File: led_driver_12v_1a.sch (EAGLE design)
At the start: 35 parts, among them Q1 BSZ0902NSI, Q2 BSZ0902NSI, Q3 BSZ0902NSI, Q4 BSZ0902NSI, Q5 BSZ0902NSI

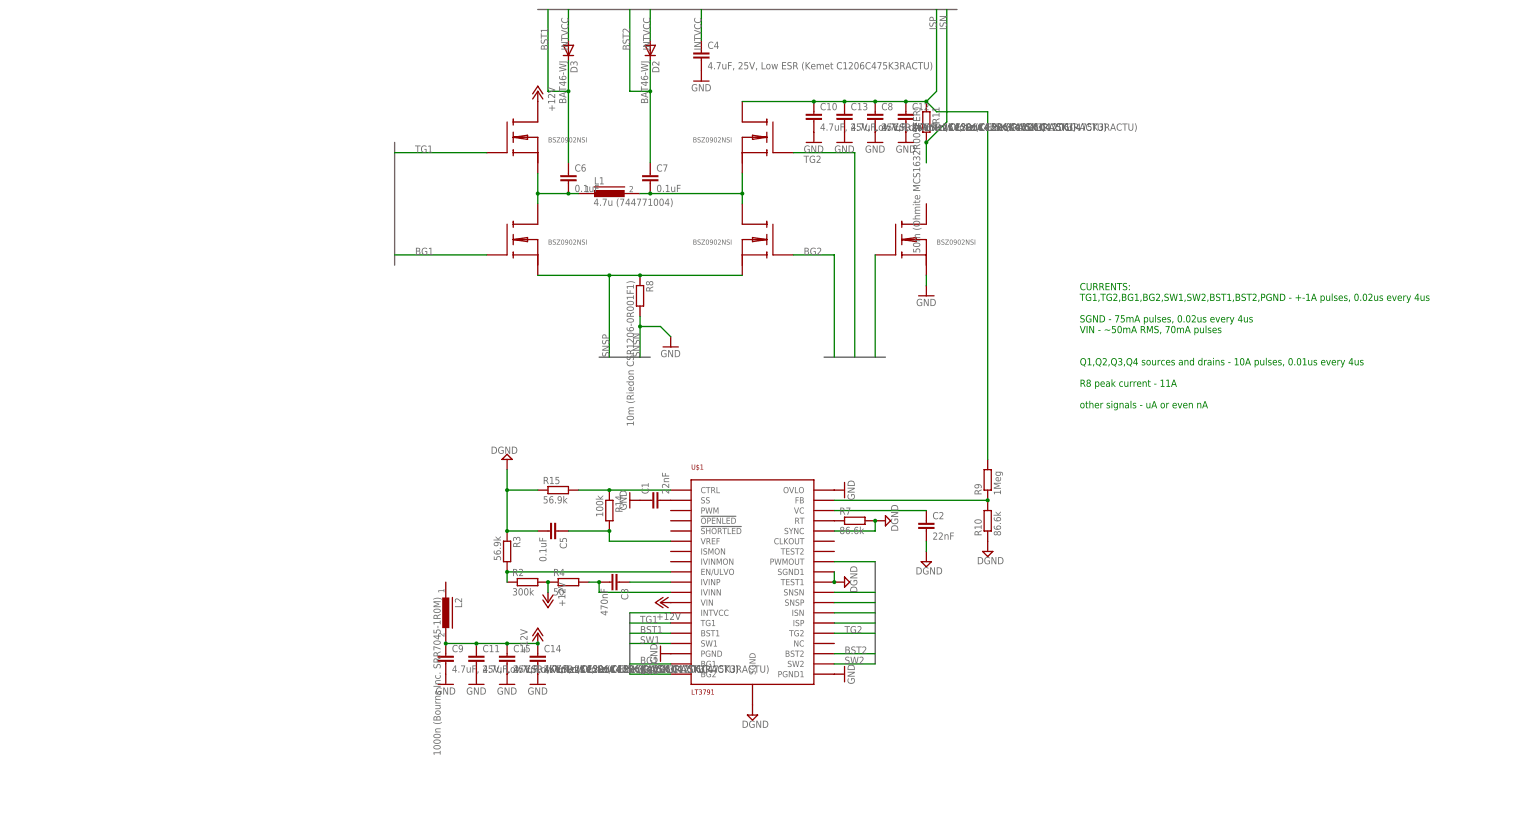
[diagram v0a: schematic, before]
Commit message: schematics roughly finished, components are roughly in place. Need accurate routing and fine component adjustments
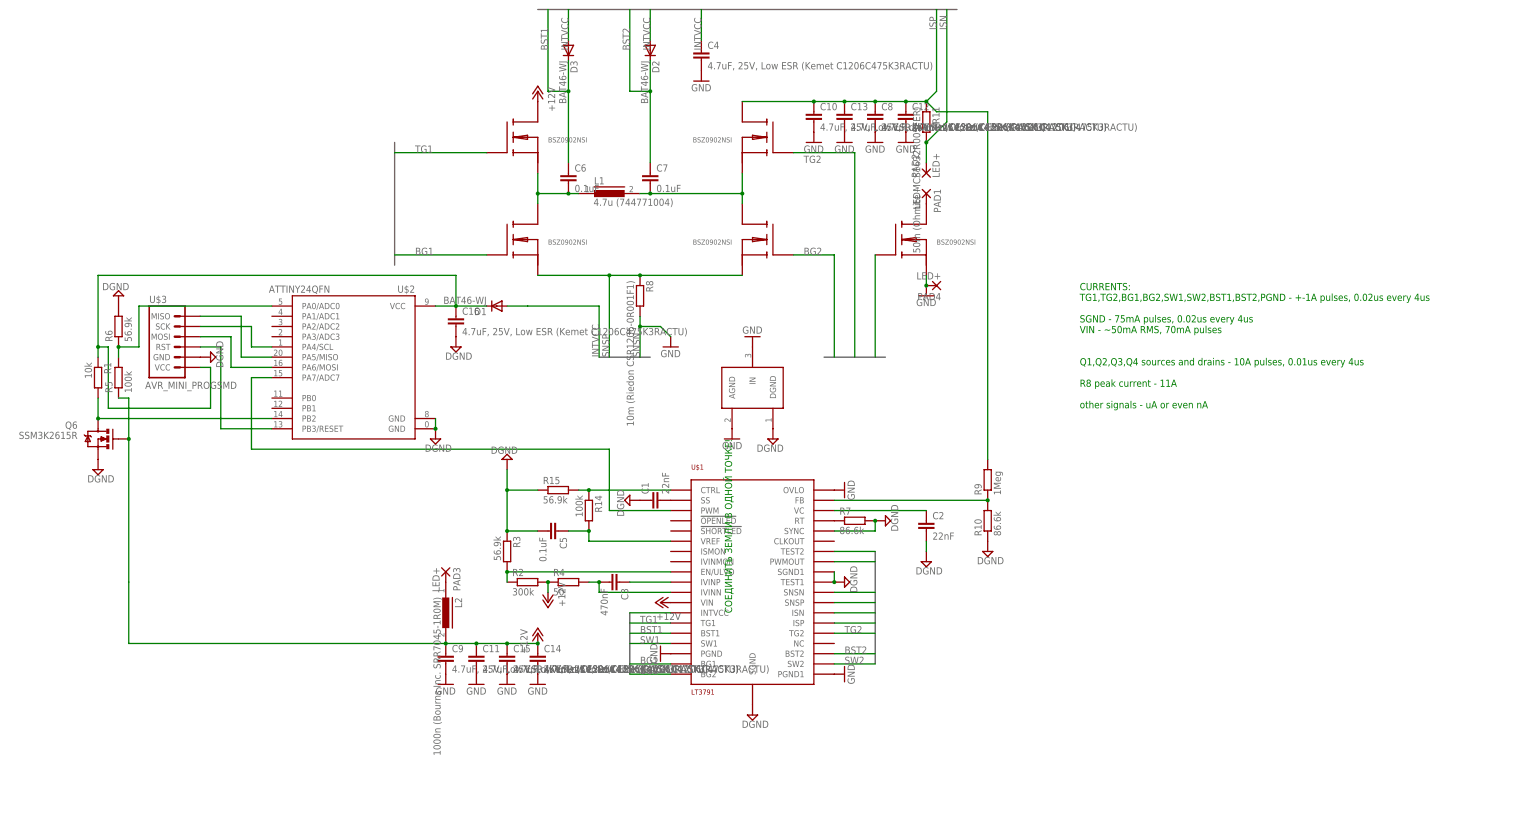
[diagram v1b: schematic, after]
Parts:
- added C16: 4.7uF, 25V, Low ESR (Kemet C1206C475K3RACTU), rcl:C-EUC1206
- added D1: BAT46-WJ, diode:DIODE-SOD323-W
- added PAD1: LED-, wirepad:WIREPADSMD5-2,5
- added PAD2, PAD3, PAD4: LED+, wirepad:WIREPADSMD5-2,5
- added Q6: SSM3K2615R, SparkFun-DiscreteSemi:MOSFET-NCHANNELBSS123LT1G
- added R1: 10k, resistor:R-EU_R0402
- added R5: 100k, resistor:R-EU_R0402
- added R6: 56.9k, resistor:R-EU_R0402
- added U$2: ATTINY24QFN, SparkFun-DigitalIC:ATTINY24QFN
- added U$3: AVR_MINI_PROGSMD, SparkFun-Connectors:AVR_MINI_PROGSMD
- added U$4: GND_CONNECT, SparkFun-Passives:GND_CONNECT
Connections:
- new net N$12: C16.1, D1.C, R1.1, U$2.VCC, U$3.VCC
- new net N$13: Q6.D, R1.2, U$2.PB2
- new net N$14: U$1.PWM, U$2.PA7/ADC7
- new net N$15: R5.2, R6.1, U$2.PA0/ADC0
- new net N$16: U$2.PA5/MISO, U$3.MISO
- new net N$17: U$2.PA6/MOSI, U$3.MOSI
- new net N$18: U$2.PB3/RESET, U$3.RST
- new net N$19: PAD1.P, Q5.D
- new net N$20: U$2.PA4/SCL, U$3.SCK
- new net N$21: L2.1, PAD3.P
- net +12V: now also Q6.G, R5.1
- net DGND: now also C1.1, C16.2, Q6.S, R6.2, U$2.GND, U$2.GND@0, U$3.GND, U$4.DGND
- net GND: now also PAD4.P, U$4.AGND, U$4.IN; no longer C1.1
- net INTVCC: now also D1.A, U$1.TEST2
- net ISN: now also PAD2.P
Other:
- note added: "СОЕДИНИТЬ ЗЕМЛИ В ОДНОЙ ТОЧКЕ!"
- moved on the sheet: R14

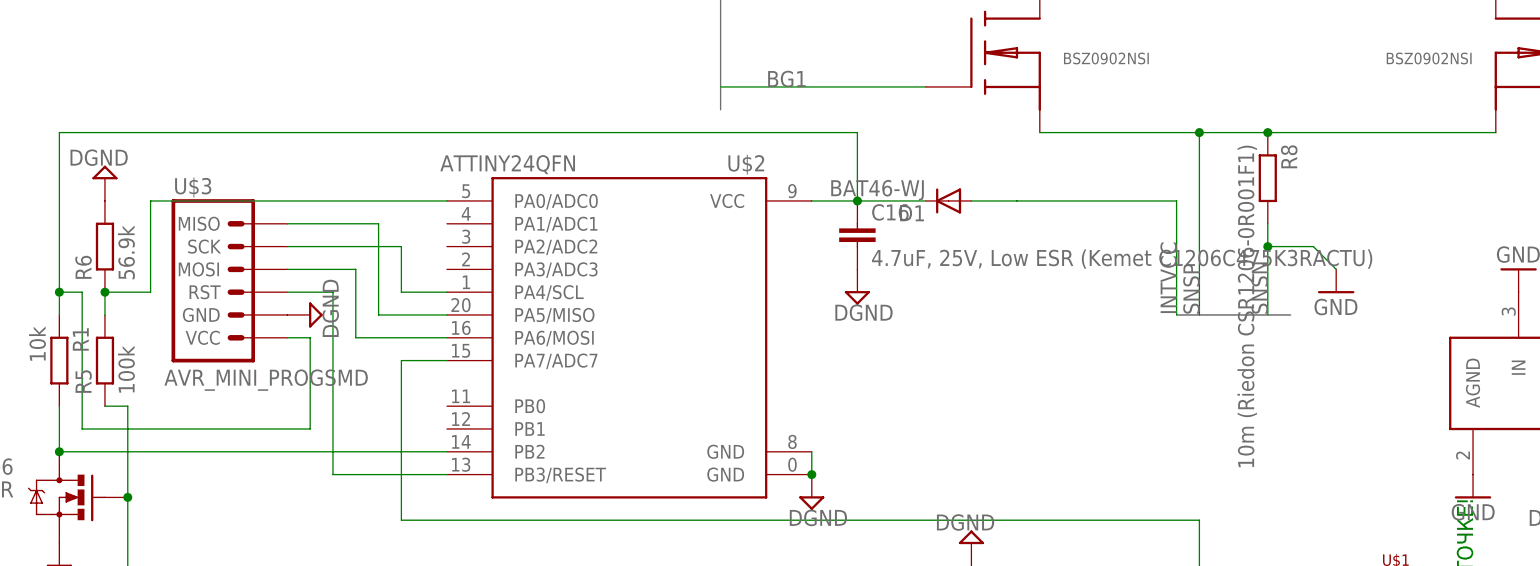
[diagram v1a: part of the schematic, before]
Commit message: second iteration of component placement. already have routing improvements, but still plenty of work to do
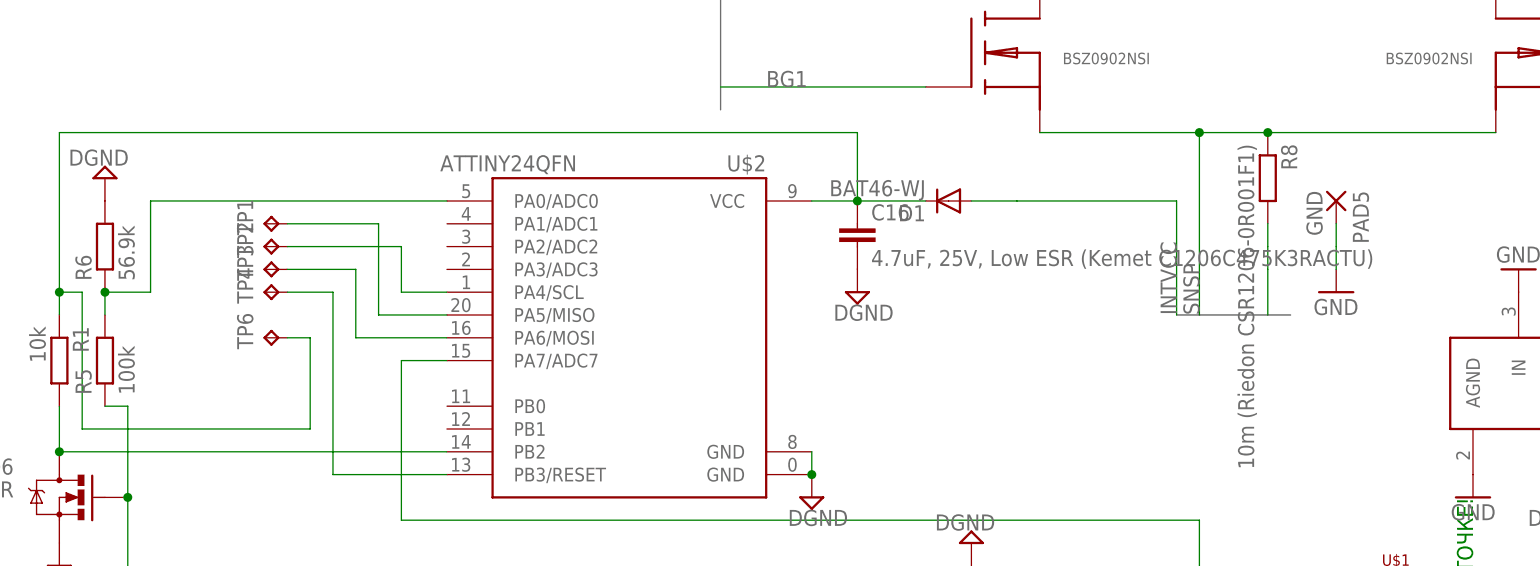
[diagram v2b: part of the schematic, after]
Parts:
- removed U$3: AVR_MINI_PROGSMD, SparkFun-Connectors:AVR_MINI_PROGSMD
- added PAD5: GND, wirepad:WIREPADSMD1,27-254
- added TP1, TP2, TP3, TP4, TP6: TPTP11R, testpad:TPTP11R
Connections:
- net DGND: no longer U$3.GND
- net GND: now also PAD5.P
- net N$12: now also TP6.TP; no longer U$3.VCC
- net N$16: now also TP1.TP; no longer U$3.MISO
- net N$17: now also TP3.TP; no longer U$3.MOSI
- net N$18: now also TP4.TP; no longer U$3.RST
- net N$20: now also TP2.TP; no longer U$3.SCK

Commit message: routing complete. main tasks to do: add polys, optimize routes width, add some extra vias, make gerbers
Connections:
- removed net N$10: C7.2, L1.2, Q3.D, Q4.S
- removed net N$8: C6.2, L1.1, Q1.S, Q2.D
- net SNSN: now also R8.1; no longer R8.2
- net SNSP: now also R8.2; no longer R8.1
- net SW1: now also C6.2, L1.1, Q1.S, Q2.D
- net SW2: now also C7.2, L1.2, Q3.D, Q4.S
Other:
- moved on the sheet: R8
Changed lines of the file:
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@@
 <clearance class="0" value="0.1524"/>
 </class>
-<class number="1" name="HI_PWR" width="0.3" drill="0.5">
+<class number="1" name="HI_PWR" width="0.3" drill="0.4">
 <clearance class="1" value="0.15"/>
 </class>
@@
 <instance part="Q3" gate="G$1" x="5.08" y="50.8" rot="MR0"/>
 <instance part="Q5" gate="G$1" x="45.72" y="50.8"/>
-<instance part="R8" gate="G$1" x="-22.86" y="38.1" rot="R270"/>
+<instance part="R8" gate="G$1" x="-22.86" y="35.56" rot="R90"/>
 <instance part="R11" gate="G$1" x="48.26" y="81.28" rot="R270"/>
 <instance part="D2" gate="G$1" x="-20.32" y="99.06" rot="R270"/>
@@
 <wire x1="25.4" y1="48.26" x2="25.4" y2="22.86" width="0.1524" layer="91"/>
 <label x="17.78" y="48.26" size="1.778" layer="95"/>
+<label x="25.4" y="25.4" size="1.778" layer="95" rot="R90"/>
 </segment>
 </net>
@@
 </segment>
 </net>
-<net name="SW2" class="0">
+<net name="SW2" class="1">
 <segment>
 <pinref part="U$1" gate="G$1" pin="SW2"/>
@@
 <label x="27.94" y="-53.34" size="1.778" layer="95"/>
 </segment>
-</net>
-<net name="SW1" class="0">
+<segment>
+<pinref part="L1" gate="G$1" pin="2"/>
+<pinref part="C7" gate="G$1" pin="2"/>
+<wire x1="-22.86" y1="63.5" x2="-20.32" y2="63.5" width="0.1524" layer="91"/>
+<pinref part="Q4" gate="G$1" pin="S"/>
+<wire x1="-20.32" y1="63.5" x2="2.54" y2="63.5" width="0.1524" layer="91"/>
+<wire x1="2.54" y1="63.5" x2="2.54" y2="68.58" width="0.1524" layer="91"/>
+<junction x="-20.32" y="63.5"/>
+<pinref part="Q3" gate="G$1" pin="D"/>
+<wire x1="2.54" y1="63.5" x2="2.54" y2="60.96" width="0.1524" layer="91"/>
+<junction x="2.54" y="63.5"/>
+<wire x1="27.94" y1="22.86" x2="27.94" y2="63.5" width="0.1524" layer="91"/>
+<wire x1="27.94" y1="63.5" x2="2.54" y2="63.5" width="0.1524" layer="91"/>
+<label x="27.94" y="25.4" size="1.778" layer="95" rot="R90"/>
+</segment>
+</net>
+<net name="SW1" class="1">
 <segment>
 <pinref part="U$1" gate="G$1" pin="SW1"/>
 <wire x1="-15.24" y1="-48.26" x2="-25.4" y2="-48.26" width="0.1524" layer="91"/>
 <label x="-22.86" y="-48.26" size="1.778" layer="95"/>
+</segment>
+<segment>
+<pinref part="Q1" gate="G$1" pin="S"/>
+<pinref part="Q2" gate="G$1" pin="D"/>
+<wire x1="-48.26" y1="68.58" x2="-48.26" y2="63.5" width="0.1524" layer="91"/>
+<pinref part="L1" gate="G$1" pin="1"/>
+<wire x1="-48.26" y1="63.5" x2="-48.26" y2="60.96" width="0.1524" layer="91"/>
+<wire x1="-38.1" y1="63.5" x2="-40.64" y2="63.5" width="0.1524" layer="91"/>
+<junction x="-48.26" y="63.5"/>
+<pinref part="C6" gate="G$1" pin="2"/>
+<wire x1="-40.64" y1="63.5" x2="-48.26" y2="63.5" width="0.1524" layer="91"/>
+<junction x="-40.64" y="63.5"/>
+<wire x1="-83.82" y1="63.5" x2="-48.26" y2="63.5" width="0.1524" layer="91"/>
+<label x="-78.74" y="63.5" size="1.778" layer="95"/>
 </segment>
 </net>
@@
 <wire x1="30.48" y1="73.66" x2="30.48" y2="22.86" width="0.1524" layer="91"/>
 <label x="17.78" y="71.12" size="1.778" layer="95"/>
+<label x="30.48" y="25.4" size="1.778" layer="95" rot="R90"/>
 </segment>
 </net>
@@
 </segment>
 </net>
-<net name="N$8" class="1">
-<segment>
-<pinref part="Q1" gate="G$1" pin="S"/>
-<pinref part="Q2" gate="G$1" pin="D"/>
-<wire x1="-48.26" y1="68.58" x2="-48.26" y2="63.5" width="0.1524" layer="91"/>
-<pinref part="L1" gate="G$1" pin="1"/>
-<wire x1="-48.26" y1="63.5" x2="-48.26" y2="60.96" width="0.1524" layer="91"/>
-<wire x1="-38.1" y1="63.5" x2="-40.64" y2="63.5" width="0.1524" layer="91"/>
-<junction x="-48.26" y="63.5"/>
-<pinref part="C6" gate="G$1" pin="2"/>
-<wire x1="-40.64" y1="63.5" x2="-48.26" y2="63.5" width="0.1524" layer="91"/>
-<junction x="-40.64" y="63.5"/>
-</segment>
-</net>
-<net name="N$10" class="1">
-<segment>
-<pinref part="L1" gate="G$1" pin="2"/>
-<pinref part="C7" gate="G$1" pin="2"/>
-<wire x1="-22.86" y1="63.5" x2="-20.32" y2="63.5" width="0.1524" layer="91"/>
-<pinref part="Q4" gate="G$1" pin="S"/>
-<wire x1="-20.32" y1="63.5" x2="2.54" y2="63.5" width="0.1524" layer="91"/>
-<wire x1="2.54" y1="63.5" x2="2.54" y2="68.58" width="0.1524" layer="91"/>
-<junction x="-20.32" y="63.5"/>
-<pinref part="Q3" gate="G$1" pin="D"/>
-<wire x1="2.54" y1="63.5" x2="2.54" y2="60.96" width="0.1524" layer="91"/>
-<junction x="2.54" y="63.5"/>
-</segment>
-</net>
 <net name="PWMOUT" class="1">
 <segment>
@@
 <pinref part="Q5" gate="G$1" pin="G"/>
 <wire x1="35.56" y1="48.26" x2="35.56" y2="22.86" width="0.1524" layer="91"/>
+<label x="35.56" y="25.4" size="1.778" layer="95" rot="R90"/>
 </segment>
 </net>
@@
 </segment>
 <segment>
-<pinref part="R8" gate="G$1" pin="2"/>
 <wire x1="-22.86" y1="22.86" x2="-22.86" y2="27.94" width="0.1524" layer="91"/>
-<wire x1="-22.86" y1="27.94" x2="-22.86" y2="30.48" width="0.1524" layer="91"/>
-<wire x1="-22.86" y1="30.48" x2="-22.86" y2="33.02" width="0.1524" layer="91"/>
+<pinref part="R8" gate="G$1" pin="1"/>
+<wire x1="-22.86" y1="30.48" x2="-22.86" y2="27.94" width="0.1524" layer="91"/>
+<label x="-22.86" y="22.86" size="1.778" layer="95" rot="R90"/>
 </segment>
 </net>
@@
 <segment>
 <pinref part="Q2" gate="G$1" pin="S"/>
+<wire x1="-48.26" y1="43.18" x2="-30.48" y2="43.18" width="0.1524" layer="91"/>
+<wire x1="-30.48" y1="22.86" x2="-30.48" y2="43.18" width="0.1524" layer="91"/>
+<label x="-30.48" y="22.86" size="1.778" layer="95" rot="R90"/>
 <pinref part="Q3" gate="G$1" pin="S"/>
-<wire x1="-48.26" y1="43.18" x2="-30.48" y2="43.18" width="0.1524" layer="91"/>
-<pinref part="R8" gate="G$1" pin="1"/>
 <wire x1="-30.48" y1="43.18" x2="-22.86" y2="43.18" width="0.1524" layer="91"/>
+<junction x="-30.48" y="43.18"/>
+<pinref part="R8" gate="G$1" pin="2"/>
 <wire x1="-22.86" y1="43.18" x2="2.54" y2="43.18" width="0.1524" layer="91"/>
+<wire x1="-22.86" y1="40.64" x2="-22.86" y2="43.18" width="0.1524" layer="91"/>
 <junction x="-22.86" y="43.18"/>
-<wire x1="-30.48" y1="22.86" x2="-30.48" y2="43.18" width="0.1524" layer="91"/>
-<junction x="-30.48" y="43.18"/>
-<label x="-30.48" y="22.86" size="1.778" layer="95" rot="R90"/>
-</segment>
-</net>
+</segment>
+</net>

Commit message: Added Gerbers and PartList
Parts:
- C16, C4: value 4.7uF, 25V, Low ESR (Kemet C1206C475K3RACTU) -> 4.7uF
- renumbered TP1 to MISO, TP2 to SCK, TP3 to MOSI, TP4 to RST, TP6 to VCC
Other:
- note removed: "CURRENTS: TG1,TG2,BG1,BG2,SW1,SW2,BST1,BST2,PGND - +-1A pulses, 0.02us every 4us SGND - 75mA pulses, 0.02us every 4us VIN - ~50mA RMS, 70mA pulses Q1,Q2,Q3,Q4 sources and drains - 10A pulses, 0.01us every 4us R8 peak current - 11A other signals - uA or even nA"
- note removed: "СОЕДИНИТЬ ЗЕМЛИ В ОДНОЙ ТОЧКЕ!"
